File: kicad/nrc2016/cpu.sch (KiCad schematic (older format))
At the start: 9 parts, among them SW1 RESET, U1 Z80CPU, U2 DIP_OSCILLATOR

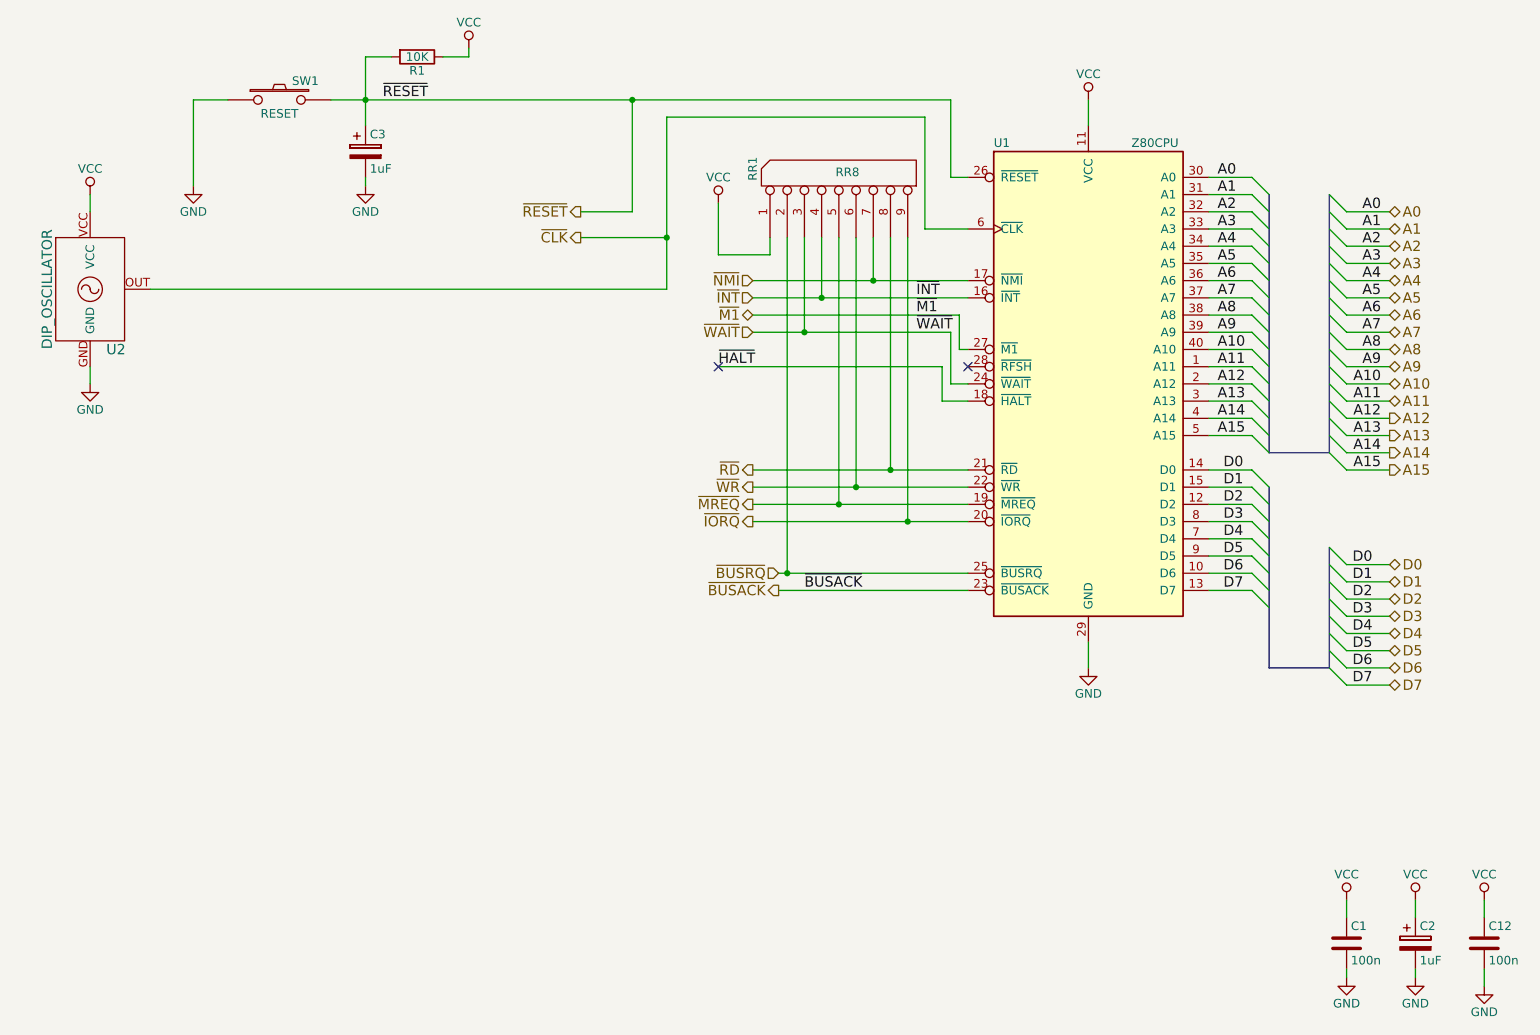
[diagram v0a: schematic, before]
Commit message: Update nrc2016 schema and PCB to use new library symbols
I've added proper schematic symbols for the pre-defined bus sockets to
stop confusion and error by just using the generic "library" socket
component and then relying on the net names to define the pins. Screwed
me once with the VCC and GND switch around, not going to happen again.
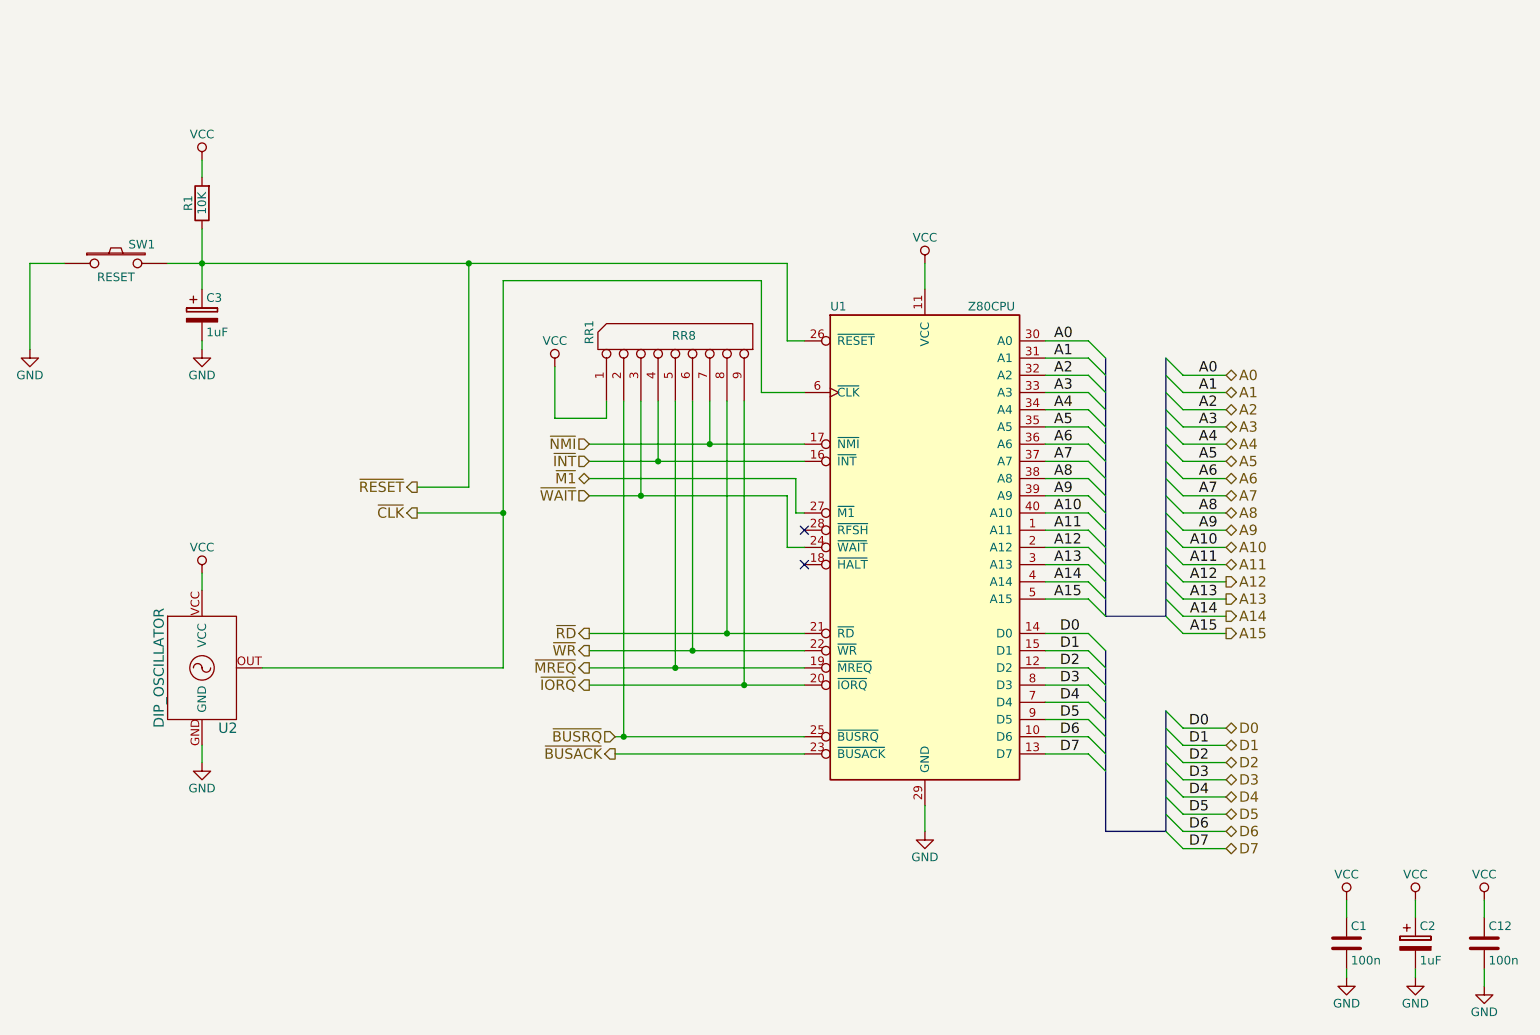
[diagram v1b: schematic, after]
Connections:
- net VCC: now also R1.2; no longer R1.1
- net ~RESET: now also R1.1; no longer R1.2
- net ~HALT: no longer names the net of U1.18 (~HALT~)
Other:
- moved on the sheet: C3, R1, RR1, SW1, U1, U2
